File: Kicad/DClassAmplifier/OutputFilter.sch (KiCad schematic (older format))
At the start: 2 parts

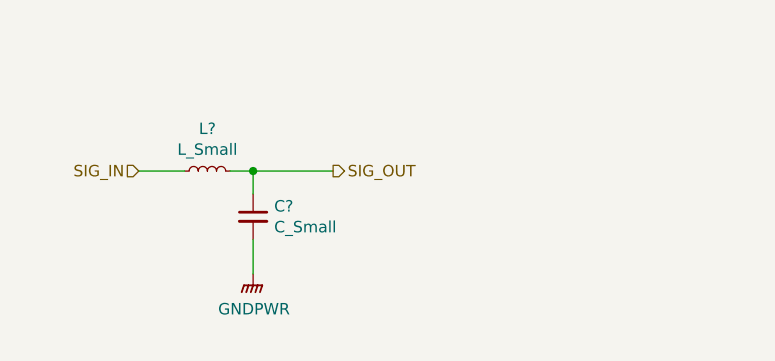
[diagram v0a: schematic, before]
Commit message: Finish off Main Part of Schematic
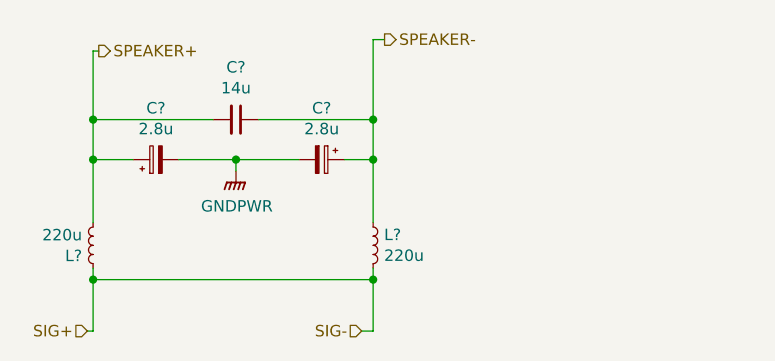
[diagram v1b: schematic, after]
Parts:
- removed C?: C_Small, symbol Device:C_Small
- removed L?: L_Small, symbol Device:L_Small
- added C?: 14u, OutputFilmCapacitor:C4AQQBW5140A3JJ, symbol Device:C_Small
- added C? (x2): 2.8u, Capacitor_THT:CP_Radial_D8.0mm_P3.50mm, symbol Device:CP_Small
- added L? (x2): 220u, 1422455C:1422455C, symbol Device:L_Small
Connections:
- net GNDPWR: now also C?.2, C?.2
- new net SIG+: L?.1, L?.2
- new net SPEAKER+: C?.1, C?.2, L?.2
- new net SPEAKER-: C?.1, C?.1, L?.1
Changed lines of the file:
@@
 $Descr A4 11693 8268
 encoding utf-8
-Sheet 2 9
+Sheet 2 7
 Title ""
 Date ""
@@
 $Comp
 L Device:L_Small L?
-U 1 1 60FD558D
-P 5250 2900
-AR Path="/60F78807/60FD558D" Ref="L?"  Part="1"
-AR Path="/610505A7/60FD558D" Ref="L?"  Part="1"
-F 0 "L?" V 5435 2900 50  0000 C CNN
-F 1 "L_Small" V 5344 2900 50  0000 C CNN
-F 2 "" H 5250 2900 50  0001 C CNN
-F 3 "~" H 5250 2900 50  0001 C CNN
-	1    5250 2900
-	0    -1   -1   0
+U 1 1 61155806
+P 5975 3225
+F 0 "L?" H 6023 3271 50  0000 L CNN
+F 1 "220u" H 6023 3180 50  0000 L CNN
+F 2 "1422455C:1422455C" H 5975 3225 50  0001 C CNN
+F 3 "~" H 5975 3225 50  0001 C CNN
+	1    5975 3225
+	1    0    0    -1
 $EndComp
 $Comp
 L Device:C_Small C?
-U 1 1 60FD5F2D
-P 5450 3100
-AR Path="/60F78807/60FD5F2D" Ref="C?"  Part="1"
-AR Path="/610505A7/60FD5F2D" Ref="C?"  Part="1"
-F 0 "C?" H 5542 3146 50  0000 L CNN
-F 1 "C_Small" H 5542 3055 50  0000 L CNN
-F 2 "" H 5450 3100 50  0001 C CNN
-F 3 "~" H 5450 3100 50  0001 C CNN
-	1    5450 3100
+U 1 1 61156022
+P 5375 2675
+F 0 "C?" V 5146 2675 50  0000 C CNN
+F 1 "14u" V 5237 2675 50  0000 C CNN
+F 2 "OutputFilmCapacitor:C4AQQBW5140A3JJ" H 5375 2675 50  0001 C CNN
+F 3 "~" H 5375 2675 50  0001 C CNN
+	1    5375 2675
+	0    1    1    0
+$EndComp
+$Comp
+L Device:CP_Small C?
+U 1 1 61156A03
+P 5750 2850
+F 0 "C?" V 5525 2850 50  0000 C CNN
+F 1 "2.8u" V 5616 2850 50  0000 C CNN
+F 2 "Capacitor_THT:CP_Radial_D8.0mm_P3.50mm" H 5750 2850 50  0001 C CNN
+F 3 "~" H 5750 2850 50  0001 C CNN
+	1    5750 2850
+	0    1    1    0
+$EndComp
+Wire Wire Line
+	4750 3125 4750 2850
+Wire Wire Line
+	4750 2850 4925 2850
+Wire Wire Line
+	5125 2850 5375 2850
+Wire Wire Line
+	5850 2850 5975 2850
+Wire Wire Line
+	5975 2850 5975 3125
+Wire Wire Line
+	5975 3325 5975 3375
+Wire Wire Line
+	5975 3375 4750 3375
+Wire Wire Line
+	4750 3375 4750 3325
+Wire Wire Line
+	5275 2675 4750 2675
+Wire Wire Line
+	4750 2675 4750 2850
+Connection ~ 4750 2850
+Wire Wire Line
+	5475 2675 5975 2675
+Wire Wire Line
+	5975 2675 5975 2850
+Connection ~ 5975 2850
+Text HLabel 4725 3600 0    50   Input ~ 0
+SIG+
+Text HLabel 5925 3600 0    50   Input ~ 0
+SIG-
+Text HLabel 4775 2375 2    50   Output ~ 0
+SPEAKER+
+Text HLabel 6025 2325 2    50   Output ~ 0
+SPEAKER-
+Wire Wire Line
+	6025 2325 5975 2325
+Wire Wire Line
+	5975 2325 5975 2675
+Connection ~ 5975 2675
+Wire Wire Line
+	4775 2375 4750 2375
+Wire Wire Line
+	4750 2375 4750 2675
+Connection ~ 4750 2675
+Wire Wire Line
+	4750 3375 4750 3600
+Wire Wire Line
+	4750 3600 4725 3600
+Connection ~ 4750 3375
+Wire Wire Line
+	5975 3375 5975 3600
+Wire Wire Line
+	5975 3600 5925 3600
+Connection ~ 5975 3375
+$Comp
+L power:GNDPWR #PWR?
+U 1 1 6115D61E
+P 5375 2900
+F 0 "#PWR?" H 5375 2700 50  0001 C CNN
+F 1 "GNDPWR" H 5379 2746 50  0000 C CNN
+F 2 "" H 5375 2850 50  0001 C CNN
+F 3 "" H 5375 2850 50  0001 C CNN
+	1    5375 2900
 	1    0    0    -1
 $EndComp
 Wire Wire Line
-	5450 3000 5450 2900
+	5375 2900 5375 2850
+Connection ~ 5375 2850
 Wire Wire Line
-	5450 2900 5350 2900
+	5375 2850 5650 2850
 $Comp
-L power:GNDPWR #PWR?
-U 1 1 60FD65BB
-P 5450 3350
-AR Path="/60F78807/60FD65BB" Ref="#PWR?"  Part="1"
-AR Path="/610505A7/60FD65BB" Ref="#PWR?"  Part="1"
-F 0 "#PWR?" H 5450 3150 50  0001 C CNN
-F 1 "GNDPWR" H 5454 3196 50  0000 C CNN
-F 2 "" H 5450 3300 50  0001 C CNN
-F 3 "" H 5450 3300 50  0001 C CNN
-	1    5450 3350
-	1    0    0    -1
+L Device:L_Small L?
+U 1 1 61202529
+P 4750 3225
+F 0 "L?" H 4798 3271 50  0000 L CNN
+F 1 "220u" H 4798 3180 50  0000 L CNN
+F 2 "1422455C:1422455C" H 4750 3225 50  0001 C CNN
+F 3 "~" H 4750 3225 50  0001 C CNN
+	1    4750 3225
+	-1   0    0    1
 $EndComp
-Wire Wire Line
-	5450 3350 5450 3200
-Text HLabel 4950 2900 0    50   Input ~ 0
-SIG_IN
-Wire Wire Line
-	4950 2900 5150 2900
-Text HLabel 5800 2900 2    50   Output ~ 0
-SIG_OUT
-Wire Wire Line
-	5800 2900 5450 2900
-Connection ~ 5450 2900
+$Comp
+L Device:CP_Small C?
+U 1 1 61203FC8
+P 5025 2850
+F 0 "C?" V 5250 2850 50  0000 C CNN
+F 1 "2.8u" V 5159 2850 50  0000 C CNN
+F 2 "Capacitor_THT:CP_Radial_D8.0mm_P3.50mm" H 5025 2850 50  0001 C CNN
+F 3 "~" H 5025 2850 50  0001 C CNN
+	1    5025 2850
+	0    -1   -1   0
+$EndComp
 $EndSCHEMATC

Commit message: updates to schematic
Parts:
- added J1: Conn_01x02, symbol Connector_Generic:Conn_01x02
- gave numbers to parts that had none: 5
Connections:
- net SIG+: no longer L2.2
- net SPEAKER+: now also J1.1 (Pin_1)
- net SPEAKER-: now also J1.2 (Pin_2)
- new net SIG-: L2.2
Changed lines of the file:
@@
 $EndDescr
 $Comp
-L Device:L_Small L?
+L Device:L_Small L2
 U 1 1 61155806
 P 5975 3225
-F 0 "L?" H 6023 3271 50  0000 L CNN
+F 0 "L2" H 6023 3271 50  0000 L CNN
 F 1 "220u" H 6023 3180 50  0000 L CNN
 F 2 "1422455C:1422455C" H 5975 3225 50  0001 C CNN
@@
 $EndComp
 $Comp
-L Device:C_Small C?
+L Device:C_Small C4
 U 1 1 61156022
 P 5375 2675
-F 0 "C?" V 5146 2675 50  0000 C CNN
+F 0 "C4" V 5146 2675 50  0000 C CNN
 F 1 "14u" V 5237 2675 50  0000 C CNN
 F 2 "OutputFilmCapacitor:C4AQQBW5140A3JJ" H 5375 2675 50  0001 C CNN
@@
 $EndComp
 $Comp
-L Device:CP_Small C?
+L Device:CP_Small C5
 U 1 1 61156A03
 P 5750 2850
-F 0 "C?" V 5525 2850 50  0000 C CNN
+F 0 "C5" V 5525 2850 50  0000 C CNN
 F 1 "2.8u" V 5616 2850 50  0000 C CNN
 F 2 "Capacitor_THT:CP_Radial_D8.0mm_P3.50mm" H 5750 2850 50  0001 C CNN
@@
 	5975 2850 5975 3125
 Wire Wire Line
-	5975 3325 5975 3375
-Wire Wire Line
-	5975 3375 4750 3375
-Wire Wire Line
-	4750 3375 4750 3325
-Wire Wire Line
 	5275 2675 4750 2675
 Wire Wire Line
@@
 Text HLabel 5925 3600 0    50   Input ~ 0
 SIG-
-Text HLabel 4775 2375 2    50   Output ~ 0
+Text HLabel 7150 2625 2    50   Output ~ 0
 SPEAKER+
-Text HLabel 6025 2325 2    50   Output ~ 0
+Text HLabel 7150 2725 2    50   Output ~ 0
 SPEAKER-
 Wire Wire Line
@@
 Connection ~ 4750 2675
 Wire Wire Line
-	4750 3375 4750 3600
-Wire Wire Line
 	4750 3600 4725 3600
-Connection ~ 4750 3375
-Wire Wire Line
-	5975 3375 5975 3600
 Wire Wire Line
 	5975 3600 5925 3600
-Connection ~ 5975 3375
 $Comp
-L power:GNDPWR #PWR?
+L power:GNDPWR #PWR0105
 U 1 1 6115D61E
 P 5375 2900
-F 0 "#PWR?" H 5375 2700 50  0001 C CNN
+F 0 "#PWR0105" H 5375 2700 50  0001 C CNN
 F 1 "GNDPWR" H 5379 2746 50  0000 C CNN
 F 2 "" H 5375 2850 50  0001 C CNN
@@
 	5375 2850 5650 2850
 $Comp
-L Device:L_Small L?
+L Device:L_Small L1
 U 1 1 61202529
 P 4750 3225
-F 0 "L?" H 4798 3271 50  0000 L CNN
+F 0 "L1" H 4798 3271 50  0000 L CNN
 F 1 "220u" H 4798 3180 50  0000 L CNN
 F 2 "1422455C:1422455C" H 4750 3225 50  0001 C CNN
@@
 $EndComp
 $Comp
-L Device:CP_Small C?
+L Device:CP_Small C3
 U 1 1 61203FC8
 P 5025 2850
-F 0 "C?" V 5250 2850 50  0000 C CNN
+F 0 "C3" V 5250 2850 50  0000 C CNN
 F 1 "2.8u" V 5159 2850 50  0000 C CNN
 F 2 "Capacitor_THT:CP_Radial_D8.0mm_P3.50mm" H 5025 2850 50  0001 C CNN
@@
 	0    -1   -1   0
 $EndComp
+$Comp
+L Connector_Generic:Conn_01x02 J1
+U 1 1 610FED81
+P 6950 2625
+F 0 "J1" H 7030 2617 50  0000 L CNN
+F 1 "Conn_01x02" H 7030 2526 50  0000 L CNN
+F 2 "" H 6950 2625 50  0001 C CNN
+F 3 "~" H 6950 2625 50  0001 C CNN
+	1    6950 2625
+	-1   0    0    -1
+$EndComp
+Wire Wire Line
+	5975 3325 5975 3600
+Wire Wire Line
+	4750 3325 4750 3600
+Text Label 7150 2625 0    50   ~ 0
+SPEAKER+
+Text Label 7150 2725 0    50   ~ 0
+SPEAKER-
+Text Label 4775 2375 0    50   ~ 0
+SPEAKER+
+Text Label 6025 2325 0    50   ~ 0
+SPEAKER-
 $EndSCHEMATC

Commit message: Added footprints to schematic
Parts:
- J1: footprint (none) -> Connector_PinSocket_2.54mm:PinSocket_1x02_P2.54mm_Vertical
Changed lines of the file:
@@
 F 0 "J1" H 7030 2617 50  0000 L CNN
 F 1 "Conn_01x02" H 7030 2526 50  0000 L CNN
-F 2 "" H 6950 2625 50  0001 C CNN
+F 2 "Connector_PinSocket_2.54mm:PinSocket_1x02_P2.54mm_Vertical" H 6950 2625 50  0001 C CNN
 F 3 "~" H 6950 2625 50  0001 C CNN
 	1    6950 2625

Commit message: Update Terminal Block Footprints
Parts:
- J1: footprint Connector_PinSocket_2.54mm:PinSocket_1x02_P2.54mm_Vertical -> TerminalBlock:TerminalBlock_bornier-2_P5.08mm
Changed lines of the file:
@@
 F 0 "J1" H 7030 2617 50  0000 L CNN
 F 1 "Conn_01x02" H 7030 2526 50  0000 L CNN
-F 2 "Connector_PinSocket_2.54mm:PinSocket_1x02_P2.54mm_Vertical" H 6950 2625 50  0001 C CNN
+F 2 "TerminalBlock:TerminalBlock_bornier-2_P5.08mm" H 6950 2625 50  0001 C CNN
 F 3 "~" H 6950 2625 50  0001 C CNN
 	1    6950 2625

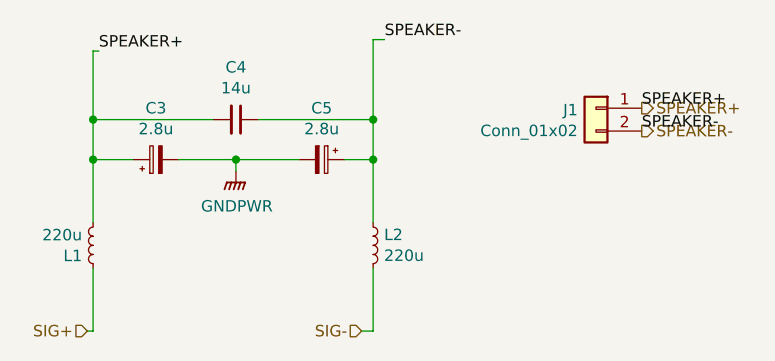
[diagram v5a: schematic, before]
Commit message: Add Test Points
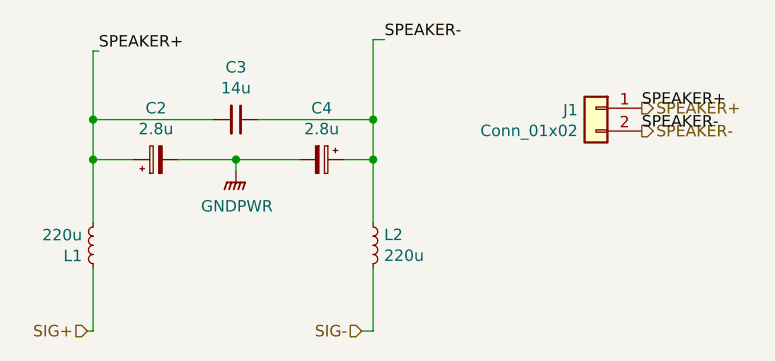
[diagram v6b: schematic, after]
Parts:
- renumbered C3 to C2, C4 to C3, C5 to C4
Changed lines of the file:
@@
 $EndComp
 $Comp
-L Device:C_Small C4
+L Device:C_Small C3
 U 1 1 61156022
 P 5375 2675
-F 0 "C4" V 5146 2675 50  0000 C CNN
+F 0 "C3" V 5146 2675 50  0000 C CNN
 F 1 "14u" V 5237 2675 50  0000 C CNN
 F 2 "OutputFilmCapacitor:C4AQQBW5140A3JJ" H 5375 2675 50  0001 C CNN
@@
 $EndComp
 $Comp
-L Device:CP_Small C5
+L Device:CP_Small C4
 U 1 1 61156A03
 P 5750 2850
-F 0 "C5" V 5525 2850 50  0000 C CNN
+F 0 "C4" V 5525 2850 50  0000 C CNN
 F 1 "2.8u" V 5616 2850 50  0000 C CNN
 F 2 "Capacitor_THT:CP_Radial_D8.0mm_P3.50mm" H 5750 2850 50  0001 C CNN
@@
 	5975 3600 5925 3600
 $Comp
-L power:GNDPWR #PWR0105
+L power:GNDPWR #PWR06
 U 1 1 6115D61E
 P 5375 2900
-F 0 "#PWR0105" H 5375 2700 50  0001 C CNN
+F 0 "#PWR06" H 5375 2700 50  0001 C CNN
 F 1 "GNDPWR" H 5379 2746 50  0000 C CNN
 F 2 "" H 5375 2850 50  0001 C CNN
@@
 $EndComp
 $Comp
-L Device:CP_Small C3
+L Device:CP_Small C2
 U 1 1 61203FC8
 P 5025 2850
-F 0 "C3" V 5250 2850 50  0000 C CNN
+F 0 "C2" V 5250 2850 50  0000 C CNN
 F 1 "2.8u" V 5159 2850 50  0000 C CNN
 F 2 "Capacitor_THT:CP_Radial_D8.0mm_P3.50mm" H 5025 2850 50  0001 C CNN

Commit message: OP Filter PCB Done
OP Filter PCB finished
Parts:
- L2: footprint 1422455C:1422455C -> OutputInductor:IND_HCTI-220-5.8
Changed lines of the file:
@@
 $Descr A4 11693 8268
 encoding utf-8
-Sheet 2 6
+Sheet 6 6
 Title ""
 Date ""
@@
 F 0 "L2" H 6023 3271 50  0000 L CNN
 F 1 "220u" H 6023 3180 50  0000 L CNN
-F 2 "1422455C:1422455C" H 5975 3225 50  0001 C CNN
+F 2 "OutputInductor:IND_HCTI-220-5.8" H 5975 3225 50  0001 C CNN
 F 3 "~" H 5975 3225 50  0001 C CNN
 	1    5975 3225

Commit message: Combined Board
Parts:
- removed J1: Conn_01x02, TerminalBlock:TerminalBlock_bornier-2_P5.08mm, symbol Connector_Generic:Conn_01x02
- C16: renamed from C3; footprint OutputFilmCapacitor:C4AQQBW5140A3JJ -> OutputFilmCapacitor:C4AQLBU5140M18K
- L1: footprint 1422455C:1422455C -> HCTI-220-5.8:IND_HCTI-220-5.8
- L2: footprint OutputInductor:IND_HCTI-220-5.8 -> HCTI-220-5.8:IND_HCTI-220-5.8
- renumbered C2 to C17, C4 to C18
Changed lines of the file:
@@
 F 0 "L2" H 6023 3271 50  0000 L CNN
 F 1 "220u" H 6023 3180 50  0000 L CNN
-F 2 "OutputInductor:IND_HCTI-220-5.8" H 5975 3225 50  0001 C CNN
+F 2 "HCTI-220-5.8:IND_HCTI-220-5.8" H 5975 3225 50  0001 C CNN
 F 3 "~" H 5975 3225 50  0001 C CNN
 	1    5975 3225
@@
 $EndComp
 $Comp
-L Device:C_Small C3
+L Device:C_Small C16
 U 1 1 61156022
 P 5375 2675
-F 0 "C3" V 5146 2675 50  0000 C CNN
+F 0 "C16" V 5146 2675 50  0000 C CNN
 F 1 "14u" V 5237 2675 50  0000 C CNN
-F 2 "OutputFilmCapacitor:C4AQQBW5140A3JJ" H 5375 2675 50  0001 C CNN
+F 2 "OutputFilmCapacitor:C4AQLBU5140M18K" H 5375 2675 50  0001 C CNN
 F 3 "~" H 5375 2675 50  0001 C CNN
 	1    5375 2675
@@
 $EndComp
 $Comp
-L Device:CP_Small C4
+L Device:CP_Small C18
 U 1 1 61156A03
 P 5750 2850
-F 0 "C4" V 5525 2850 50  0000 C CNN
+F 0 "C18" V 5525 2850 50  0000 C CNN
 F 1 "2.8u" V 5616 2850 50  0000 C CNN
 F 2 "Capacitor_THT:CP_Radial_D8.0mm_P3.50mm" H 5750 2850 50  0001 C CNN
@@
 Text HLabel 5925 3600 0    50   Input ~ 0
 SIG-
-Text HLabel 7150 2625 2    50   Output ~ 0
+Text HLabel 4775 2375 2    50   Output ~ 0
 SPEAKER+
-Text HLabel 7150 2725 2    50   Output ~ 0
+Text HLabel 6025 2325 2    50   Output ~ 0
 SPEAKER-
 Wire Wire Line
@@
 	5975 3600 5925 3600
 $Comp
-L power:GNDPWR #PWR06
+L power:GNDPWR #PWR049
 U 1 1 6115D61E
 P 5375 2900
-F 0 "#PWR06" H 5375 2700 50  0001 C CNN
+F 0 "#PWR049" H 5375 2700 50  0001 C CNN
 F 1 "GNDPWR" H 5379 2746 50  0000 C CNN
 F 2 "" H 5375 2850 50  0001 C CNN
@@
 	5375 2850 5650 2850
 $Comp
-L Device:L_Small L1
-U 1 1 61202529
-P 4750 3225
-F 0 "L1" H 4798 3271 50  0000 L CNN
-F 1 "220u" H 4798 3180 50  0000 L CNN
-F 2 "1422455C:1422455C" H 4750 3225 50  0001 C CNN
-F 3 "~" H 4750 3225 50  0001 C CNN
-	1    4750 3225
-	-1   0    0    1
-$EndComp
-$Comp
-L Device:CP_Small C2
+L Device:CP_Small C17
 U 1 1 61203FC8
 P 5025 2850
-F 0 "C2" V 5250 2850 50  0000 C CNN
+F 0 "C17" V 5250 2850 50  0000 C CNN
 F 1 "2.8u" V 5159 2850 50  0000 C CNN
 F 2 "Capacitor_THT:CP_Radial_D8.0mm_P3.50mm" H 5025 2850 50  0001 C CNN
@@
 	0    -1   -1   0
 $EndComp
-$Comp
-L Connector_Generic:Conn_01x02 J1
-U 1 1 610FED81
-P 6950 2625
-F 0 "J1" H 7030 2617 50  0000 L CNN
-F 1 "Conn_01x02" H 7030 2526 50  0000 L CNN
-F 2 "TerminalBlock:TerminalBlock_bornier-2_P5.08mm" H 6950 2625 50  0001 C CNN
-F 3 "~" H 6950 2625 50  0001 C CNN
-	1    6950 2625
-	-1   0    0    -1
-$EndComp
 Wire Wire Line
 	5975 3325 5975 3600
 Wire Wire Line
 	4750 3325 4750 3600
-Text Label 7150 2625 0    50   ~ 0
-SPEAKER+
-Text Label 7150 2725 0    50   ~ 0
-SPEAKER-
-Text Label 4775 2375 0    50   ~ 0
-SPEAKER+
-Text Label 6025 2325 0    50   ~ 0
-SPEAKER-
+$Comp
+L Device:L_Small L1
+U 1 1 61245121
+P 4750 3225
+F 0 "L1" H 4798 3271 50  0000 L CNN
+F 1 "220u" H 4798 3180 50  0000 L CNN
+F 2 "HCTI-220-5.8:IND_HCTI-220-5.8" H 4750 3225 50  0001 C CNN
+F 3 "~" H 4750 3225 50  0001 C CNN
+	1    4750 3225
+	-1   0    0    1
+$EndComp
 $EndSCHEMATC
